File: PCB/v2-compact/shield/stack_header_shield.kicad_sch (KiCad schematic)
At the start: 0 parts

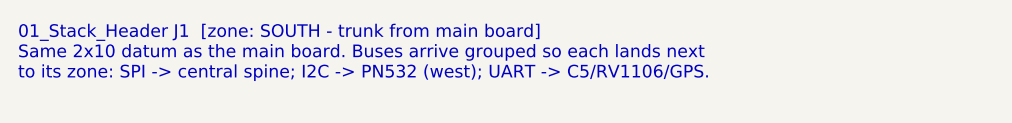
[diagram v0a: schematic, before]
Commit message: PCB: rework main board to phone-style layout; J1 -> horizontal strip
Main board (per feedback) is now a phone-style split — front is pure UI, back
carries the electronics:
- FRONT: status LEDs at the very top (above the display), TFT rotated to
  LANDSCAPE (sideways), nav buttons below it and moved down. Same feel as the
  ESP32-DIV, sideways screen.
- BACK: ESP32-S3 behind the display, microSD beside it, power + USB-C at the
  bottom-centre edge like a phone.

To keep the centre column free for the landscape display and the bottom-centre
USB-C, J1 is reoriented from a vertical 2x10 to a HORIZONTAL 10x2 strip in the
lower-centre. J1 is the shared mating datum, so the shield's J1 moves to match;
the shield's RV1106 / HTRC110 / bulk-cap zones shift to sit above/below the new
strip (SPI spine still runs north from it). Every v1 capability unchanged.

Updated both .kicad_pcb, both floorplan SVGs, both schematics' zone specs, and
PLACEMENT.md. Verified: files parse, J1 clears all zones, no same-side overlaps.

Co-Authored-By: Claude <noreply@anthropic.com>
Claude-Session: https://claude.ai/code/session_017BEAKBRVwbUCc7Sa2o3Ye7
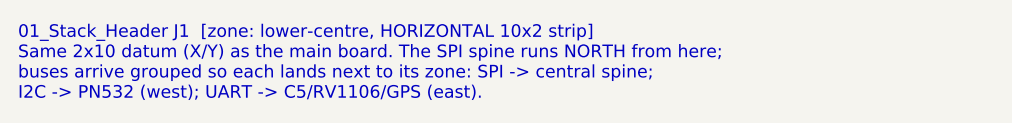
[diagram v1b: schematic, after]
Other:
- note added: "01_Stack_Header J1 [zone: lower-centre, HORIZONTAL 10x2 strip] Same 2x10 datum (X/Y) as the main board. The SPI spine runs NORTH from here; buses arrive grouped so each lands next to its zone: SPI -> central spine; I2C -> PN532 (west); UART -> C5/RV1106/GPS (east)."
- note removed: "01_Stack_Header J1 [zone: SOUTH - trunk from main board] Same 2x10 datum as the main board. Buses arrive grouped so each lands next to its zone: SPI -> central spine; I2C -> PN532 (west); UART -> C5/RV1106/GPS."
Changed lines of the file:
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@@
   (paper "A4")
   (title_block (title "01_Stack_Header") (company "YurilLAB"))
-  (text "01_Stack_Header J1  [zone: SOUTH - trunk from main board]
-Same 2x10 datum as the main board. Buses arrive grouped so each lands next
-to its zone: SPI -> central spine; I2C -> PN532 (west); UART -> C5/RV1106/GPS." (at 15 15 0)
+  (text "01_Stack_Header J1  [zone: lower-centre, HORIZONTAL 10x2 strip]
+Same 2x10 datum (X/Y) as the main board. The SPI spine runs NORTH from here;
+buses arrive grouped so each lands next to its zone: SPI -> central spine;
+I2C -> PN532 (west); UART -> C5/RV1106/GPS (east)." (at 15 15 0)
     (effects (font (size 1.4 1.4)) (justify left top)))
   (sheet_instances (path "/" (page "1")))
